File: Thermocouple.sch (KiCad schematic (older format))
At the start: 0 parts

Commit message: Finished Thermocouple Unit
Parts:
- added C?: C, ~, symbol C
- added D?: ZENER, ~, symbol ZENER
- added R? (x7): R, ~, symbol R
- added U? (x4): LM324, symbol LM324
- added U? (x2): MCP3550-60-E/SN, SO8, symbol MCP3550-60-E/SN
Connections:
- net TC IN +: now also U?.3 (+)
- net TC IN -: now also U?.3 (+)
- new net: R?.1, R?.2, U?.1
- new net: R?.1, R?.2, U?.2 (-) (x3)
- new net: R?.2, R?.2, U?.1
- new net: R?.1, U?.1, U?.2 (Vin+)
- new net: R?.1, R?.2, U?.3 (+)
- new net: U?.1, U?.2 (-), U?.2 (Vin+)
- new net +12V: D?.2 (K), U?.3 (+), U?.4 (V+), U?.4 (V+), U?.4 (V+)
- new net -12V: U?.11 (V-), U?.11 (V-), U?.11 (V-)
- new net CLK: U?.5 (SCK)
- new net CS_N: U?.7 (~CS~)
- new net GNDA: D?.1 (A), R?.1, U?.3 (Vin-), U?.3 (Vin-)
- new net MISO: U?.6 (SDO/~RDY~)
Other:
- note added: "16-24bit ADC"
- note added: "Analog/TC Input"
- note added: "General Temperature Sensor"
- note added: "Instrumentation Amp"

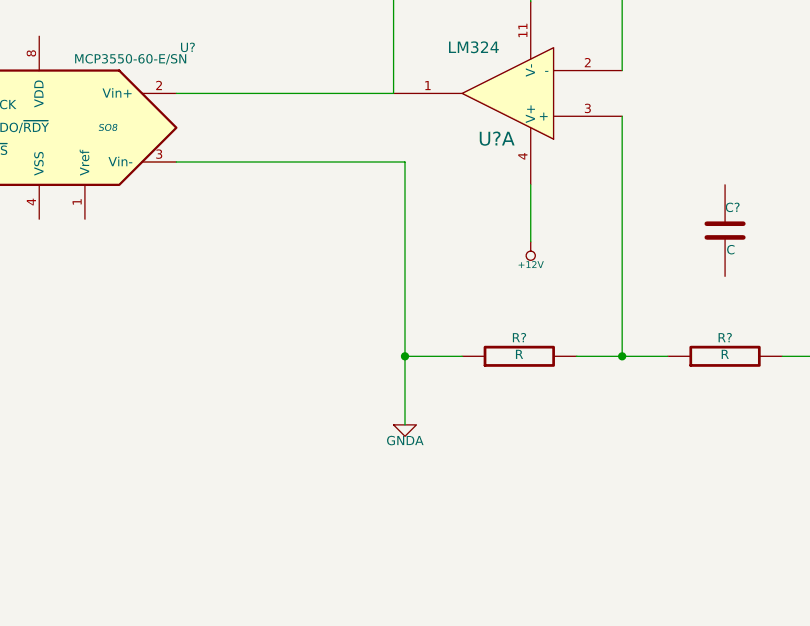
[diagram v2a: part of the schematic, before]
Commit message: Finished Week 3, Unit 7: Power Monitoring Blocks
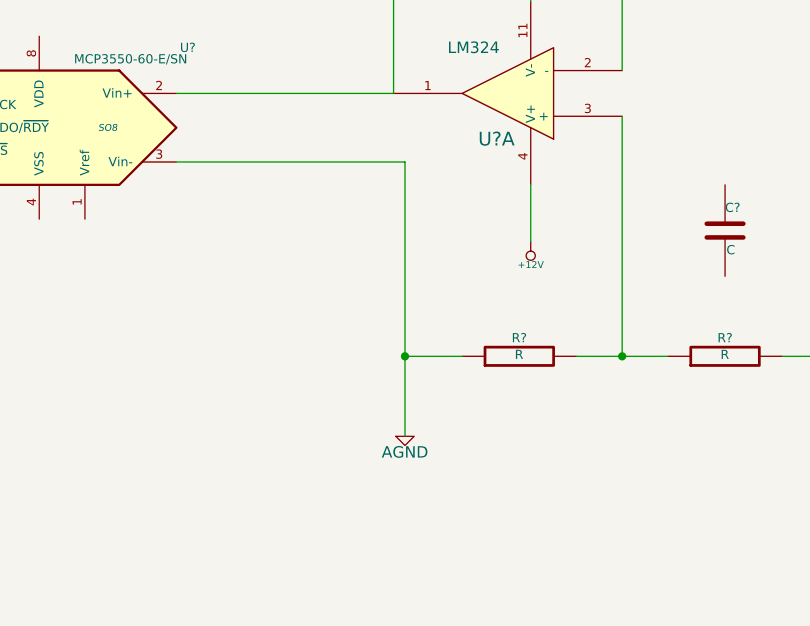
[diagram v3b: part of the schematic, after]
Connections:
- net GNDA: no longer R?.1, U?.3 (Vin-)
- new net AGND: R?.1, U?.3 (Vin-)
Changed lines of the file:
@@
 Sheet 3 9
 Title ""
-Date "5 feb 2014"
+Date "6 feb 2014"
 Rev ""
 Comp ""
@@
 Wire Wire Line
 	8300 4300 8300 4550
-$Comp
-L GNDA #PWR?
-U 1 1 52F0DC0D
-P 5200 4200
-F 0 "#PWR?" H 5200 4200 40  0001 C CNN
-F 1 "GNDA" H 5200 4130 40  0000 C CNN
-F 2 "" H 5200 4200 60  0000 C CNN
-F 3 "" H 5200 4200 60  0000 C CNN
-	1    5200 4200
-	1    0    0    -1
-$EndComp
-Wire Wire Line
-	5200 3050 5200 4200
+Wire Wire Line
+	5200 3050 5200 4250
 Wire Wire Line
 	5200 3900 5450 3900
@@
 Text Notes 3500 1950 0    60   ~ 0
 16-24bit ADC
+$Comp
+L AGND #PWR?
+U 1 1 52F3642E
+P 5200 4250
+F 0 "#PWR?" H 5200 4250 40  0001 C CNN
+F 1 "AGND" H 5200 4180 50  0000 C CNN
+F 2 "" H 5200 4250 60  0000 C CNN
+F 3 "" H 5200 4250 60  0000 C CNN
+	1    5200 4250
+	1    0    0    -1
+$EndComp
 $EndSCHEMATC
